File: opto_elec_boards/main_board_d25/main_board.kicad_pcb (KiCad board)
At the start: 2 copper layers, 66.7 x 81.9 mm, 32 parts, among them J1 IN1_BNC, J11 SWITCH_B, J12 SWITCH_C, J13 ToSlaveBoard, J2 IN2_BNC, J3 OUT1_BNC, J4 OUT2_BNC, J5 OUT3_BNC, J6 OUT4_BNC, J7 POW_+15V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

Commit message: Update OptoBoard / D25 version
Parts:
- added RV3: R_Potentiometer, Connector_PinHeader_2.54mm:PinHeader_1x03_P2.54mm_Vertical, F.Cu at (83.8, 63.0)
- J13: footprint Connector_Dsub:DSUB-25_Socket_Horizontal_P2.77x2.84mm_EdgePinOffset9.90mm_Housed_MountingHolesOffset11.32mm -> Connector_Dsub:DSUB-25_Socket_Horizontal_P2.77x2.84mm_EdgePinOffset4.94mm_Housed_MountingHolesOffset4.94mm
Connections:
- J13 pad 11: GND -> RVAR_15V
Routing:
- net RVAR_15V: track 0.00 -> 18.9 mm
- net 3.3V: track 104.4 -> 112.6 mm
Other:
- board text added: "15V"

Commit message: Update Opto D25
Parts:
- removed the G*** at (112.2, 86.8)
- added G***: LOGO, LEnsE_devices:Logo_New_Small, F.Cu at (112.3, 86.4)
- moved C2 10.1 mm to (100.1, 77.2), turned to 0 degrees
- moved J13 8.82 mm to (56.2, 88.0)
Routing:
- net SEL3: track 58.6 -> 68.4 mm
- net 3.3V: track 112.6 -> 121.6 mm
- net SEL2: track 44.2 -> 53.1 mm
- net -15V: track 56.5 -> 65.3 mm
- net IN1: track 24.4 -> 33.2 mm
- net SEL1: track 36.4 -> 45.2 mm
- net RVAR_5V: track 28.1 -> 36.9 mm
- net RVAR_15V: track 18.9 -> 27.7 mm
- net OUT3: track 13.5 -> 22.3 mm
- net OUT1: track 13.5 -> 22.3 mm
- net 5V: track 49.0 -> 57.8 mm
- net IN2: track 13.6 -> 22.4 mm
- net +15V: track 95.8 -> 104.6 mm
- net OUT4: track 24.4 -> 33.1 mm
- net OUT2: track 24.4 -> 33.1 mm
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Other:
- board size 66.7 x 81.9 mm -> 71.2 x 84.1 mm

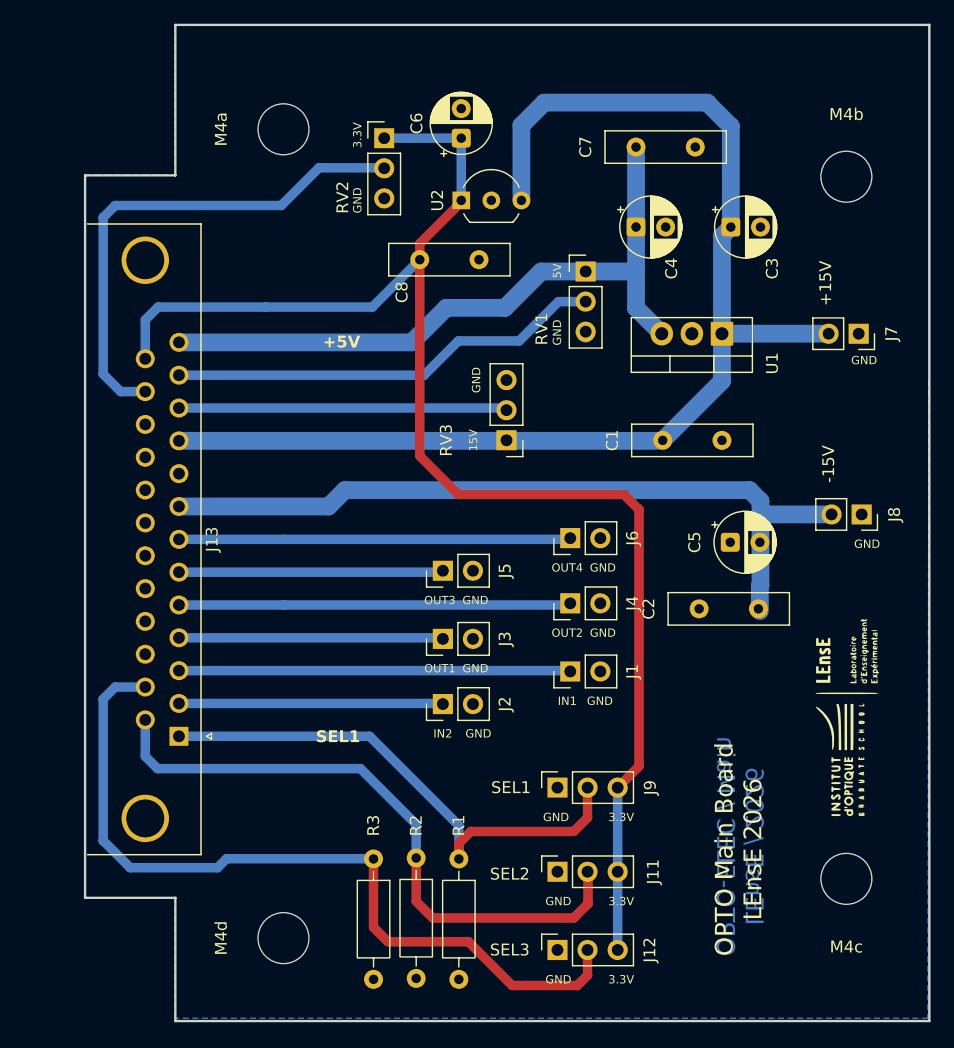
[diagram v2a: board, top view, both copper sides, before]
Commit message: Update Opto / Master and PhD Slave boards
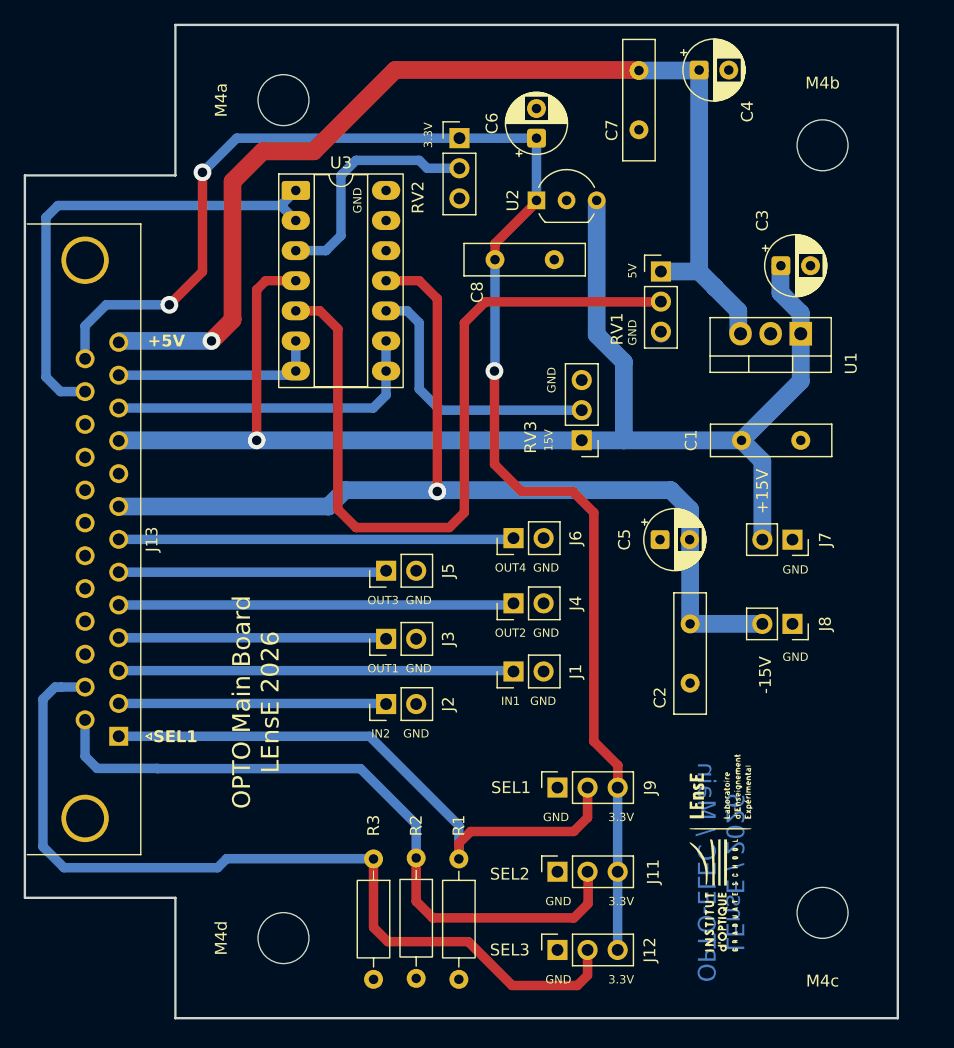
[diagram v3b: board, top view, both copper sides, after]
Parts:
- added U3: TL084, Package_DIP:DIP-14_W7.62mm_Socket_LongPads, F.Cu at (66.0, 41.9)
- moved J7 18.3 mm to (108.0, 71.4)
- moved G*** 15.6 mm to (101.6, 97.8)
- moved C4 14.3 mm to (100.1, 31.8)
- moved J8 10.9 mm to (108.0, 78.5)
- moved C1 6.65 mm to (103.7, 63.0)
- moved U1 6.65 mm to (108.7, 54.0)
- moved C7 6.46 mm to (95.0, 31.8), turned to -90 degrees
- moved RV3 6.35 mm to (90.2, 63.0)
- moved C6 6.35 mm to (86.3, 37.5)
- moved C8 6.35 mm to (82.8, 47.8)
- moved RV1 6.35 mm to (96.8, 48.8)
- moved RV2 6.35 mm to (79.8, 37.5)
- moved U2 6.35 mm to (86.3, 42.8)
- moved C2 6.32 mm to (99.3, 83.5), turned to 90 degrees
- moved C5 5.93 mm to (96.8, 71.4)
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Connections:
- RV1 pad 2: RVAR_5V -> Net-(U3B-+)
- RV2 pad 2: RVAR_3.3V -> Net-(U3A-+)
- RV3 pad 2: RVAR_15V -> Net-(U3C-+)
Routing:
- net Net-(U3B-+): track 0.00 -> 64.6 mm
- net 5V: track 57.8 -> 92.2 mm, vias 0 -> 1
- net Net-(U3C-+): track 0.00 -> 23.5 mm
- net -15V: track 65.3 -> 86.4 mm, vias 0 -> 1
- net Net-(U3A-+): track 0.00 -> 20.3 mm
- net RVAR_5V: track 36.9 -> 17.6 mm
- net +15V: track 104.6 -> 116.7 mm, vias 0 -> 1
- net 3.3V: track 121.6 -> 129.2 mm, vias 0 -> 3
- net SEL3: track 68.4 -> 73.7 mm
- net SEL2: track 53.1 -> 58.2 mm
- net SEL1: track 45.2 -> 50.3 mm
- net RVAR_3.3V: track 42.8 -> 41.1 mm
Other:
- board size 71.2 x 84.1 mm -> 73.7 x 83.8 mm
